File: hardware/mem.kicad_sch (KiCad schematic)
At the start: 3 parts, among them U6 74HC74, U7 28C256, U8 AS6C1008-xxP

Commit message: Added gpio
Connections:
- net GND: now also U6.7 (GND)
- net R/W renamed R/~{W}
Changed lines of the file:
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@@
+		)
+	)
+	(wire
+		(pts
+			(xy 133.35 146.05) (xy 137.16 146.05)
+		)
+		(stroke
+			(width 0)
+			(type default)
 		)
 	)
@@
 		)
 	)
-	(global_label "R{slash}W"
-		(shape input)
-		(at 199.39 93.98 180)
-		(fields_autoplaced yes)
-		(effects
-			(font
-				(size 1.27 1.27)
-			)
-			(justify right)
-		)
-		(property "Intersheetrefs" "${INTERSHEET_REFS}"
-			(at 192.3529 93.98 0)
-			(effects
-				(font
-					(size 1.27 1.27)
-				)
-				(justify right)
-				(hide yes)
-			)
-		)
-	)
 	(global_label "RAM_CS"
 		(shape input)
@@
 	)
 	(global_label "D[0..7]"
-		(shape input)
+		(shape bidirectional)
 		(at 68.58 106.68 180)
 		(fields_autoplaced yes)
@@
 		)
 		(property "Intersheetrefs" "${INTERSHEET_REFS}"
-			(at 59.0028 106.68 0)
+			(at 57.8915 106.68 0)
 			(effects
 				(font
@@
 			(effects
 				(font
+					(size 1.27 1.27)
+				)
+				(justify right)
+				(hide yes)
+			)
+		)
+	)
+	(global_label "R{slash}~{W}"
+		(shape input)
+		(at 199.39 93.98 180)
+		(fields_autoplaced yes)
+		(effects
+			(font
+				(size 1.27 1.27)
+			)
+			(justify right)
+		)
+		(property "Intersheetrefs" "${INTERSHEET_REFS}"
+			(at 192.3529 93.98 0)
+			(effects
+				(font

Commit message: Improved labels
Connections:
- net BANK0 renamed BANK_{0}
- net BANK1 renamed BANK_{1}
- net Bank_CS renamed BANK_{CS}
- net RAM_CS renamed RAM_{~{CS}}
- net ROM_CS renamed ROM_{~{CS}}
- no-connect marks 0 -> 2
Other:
- moved on the sheet: U6A, U6B, U6C

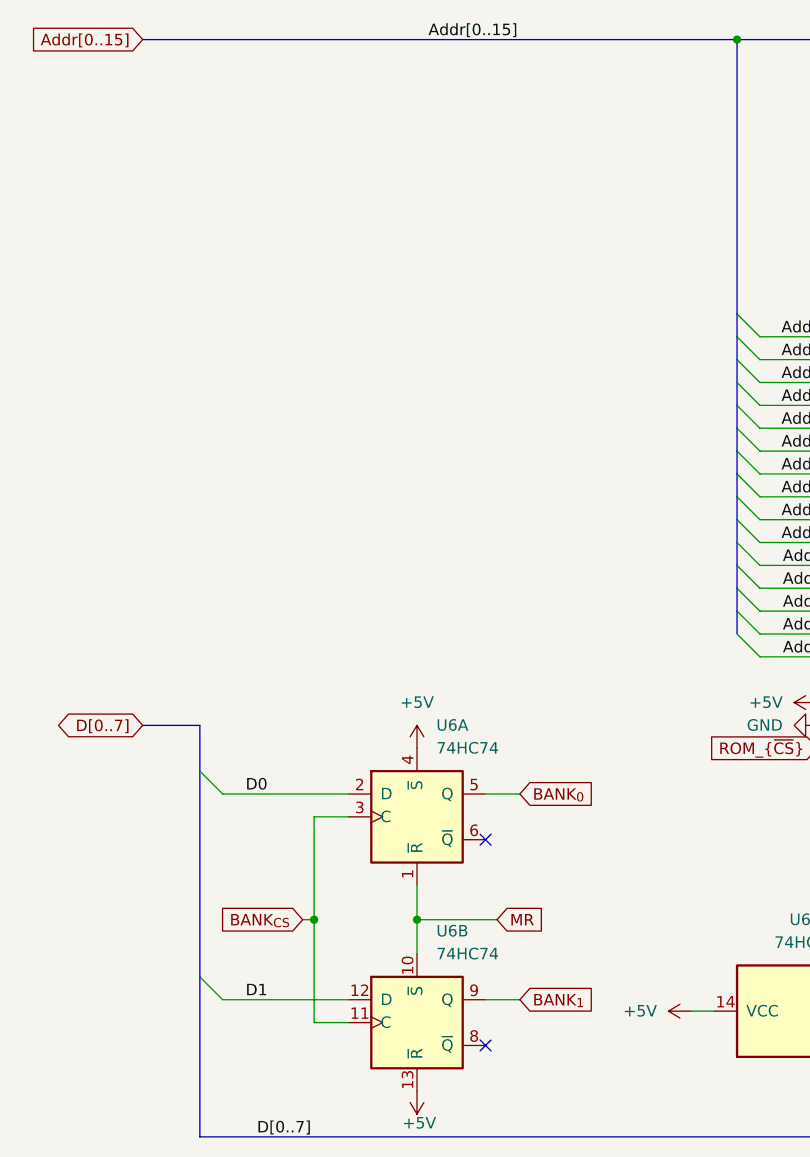
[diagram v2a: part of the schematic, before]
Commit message: Improved Schematics and added fooprints
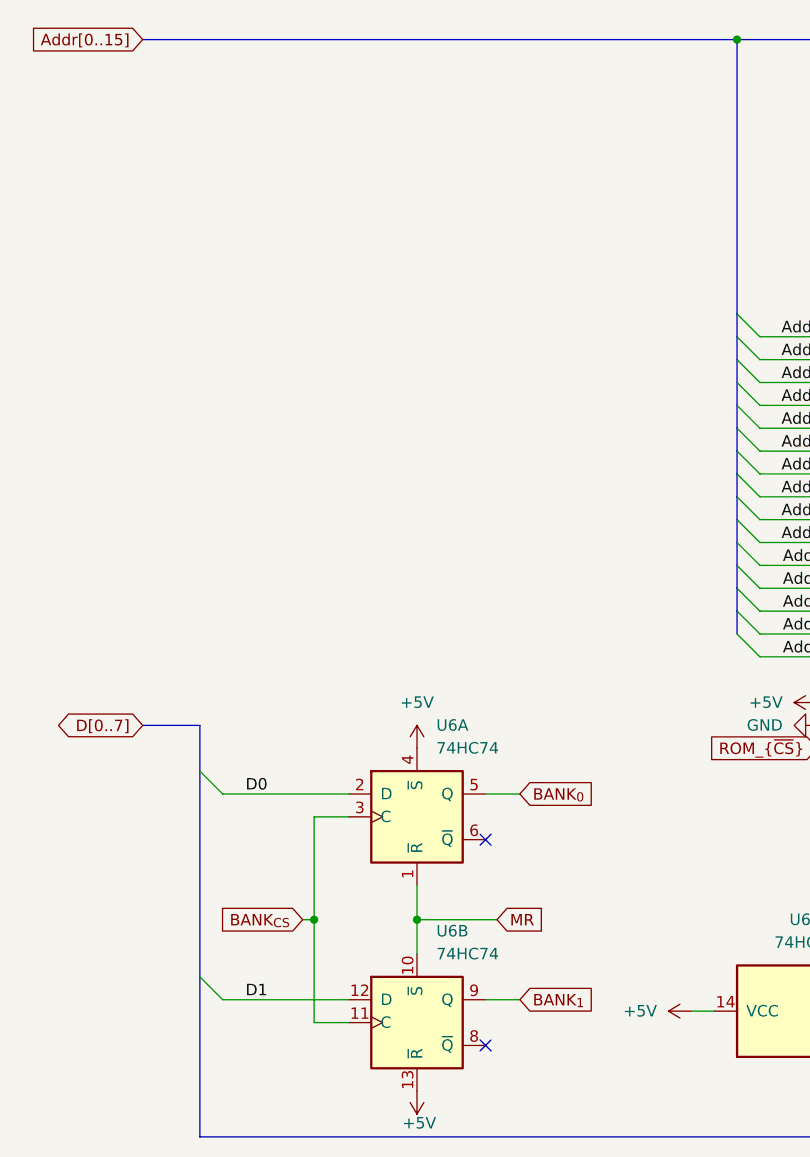
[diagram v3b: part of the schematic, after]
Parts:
- U6: footprint (none) -> Package_DIP:DIP-14_W7.62mm
- U7: footprint (none) -> AT28C256-15PU:DIP1544W45P254L3740H635Q28B
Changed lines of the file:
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@@
-		)
-	)
-	(label "D[0..7]"
-		(at 81.28 152.4 0)
-		(effects
-			(font
-				(size 1.27 1.27)
-			)
-			(justify left bottom)
 		)
 	)
@@
 			)
 			(justify right bottom)
-		)
-	)
-	(label "Addr[0..15]"
-		(at 100.33 30.48 0)
-		(effects
-			(font
-				(size 1.27 1.27)
-			)
-			(justify left bottom)
 		)
 	)
@@
 			)
 		)
-		(property "Footprint" ""
+		(property "Footprint" "Package_DIP:DIP-14_W7.62mm"
 			(at 142.24 138.43 0)
 			(effects
@@
 			)
 		)
-		(property "Footprint" ""
+		(property "Footprint" "Package_DIP:DIP-14_W7.62mm"
 			(at 99.06 116.84 0)
 			(effects
@@
 			)
 		)
-		(property "Footprint" ""
+		(property "Footprint" "AT28C256-15PU:DIP1544W45P254L3740H635Q28B"
 			(at 156.21 86.36 0)
 			(effects
@@
 			)
 		)
-		(property "Footprint" ""
+		(property "Footprint" "Package_DIP:DIP-14_W7.62mm"
 			(at 99.06 139.7 0)
 			(effects

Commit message: Added Board Register
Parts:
- removed U6: 74HC74, Package_DIP:DIP-14_W7.62mm, symbol 74xx:74HC74
- added U12: 74HC373, symbol 74xx:74HC373
- added U13: 74HCT541, symbol 74xx:74HCT541
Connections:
- net D0: now also U12.3 (D0), U13.18 (Y0)
- net D1: now also U12.4 (D1), U13.17 (Y1)
- net D2: now also U12.7 (D2), U13.16 (Y2)
- net D3: now also U12.8 (D3), U13.15 (Y3)
- net D4: now also U12.13 (D4), U13.14 (Y4)
- net D5: now also U12.14 (D5), U13.13 (Y5)
- net D6: now also U12.17 (D6), U13.12 (Y6)
- net D7: now also U12.18 (D7), U13.11 (Y7)
- net GND: now also U12.10 (GND), U13.10 (GND)
- net BANK_{0} renamed Bank_{0}
- net Bank_{0}: now also U12.2 (O0), U13.2 (A0)
- net BANK_{1} renamed Bank_{1}
- net Bank_{1}: now also U12.5 (O1), U13.3 (A1)
- new net: U12.9 (O3), U13.5 (A3)
- new net: U12.12 (O4), U13.6 (A4)
- new net: U12.15 (O5), U13.7 (A5)
- new net: U12.16 (O6), U13.8 (A6)
- new net: U12.19 (O7), U13.9 (A7)
- new net +3.3V: U12.1 (OE), U12.20 (VCC), U13.20 (VCC)
- new net BoardReg_{~{CS}}: U13.1 (G1)
- new net VBank_{2}: U12.6 (O2), U13.4 (A2)
- new net ~{R}/W: U12.11 (LE), U13.19 (G2)
- no-connect marks 2 -> 0

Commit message: Fixed some erros, changed to 3V
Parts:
- added D1, D2, D3, D4, D5, D6, D7, D8: LED, LED_SMD:LED_0805_2012Metric, symbol Device:LED
- added R16, R18, R19, R20, R21, R22, R23, R24: 470R, Resistor_SMD:R_0603_1608Metric, symbol Device:R_Small_US
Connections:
- net +3.3V: now also U7.28 (VCC), U8.32 (VCC)
- net +5V: no longer U7.28 (VCC), U8.32 (VCC)
- net Bank_{0}: now also D1.2 (A)
- net Bank_{1}: now also D2.2 (A)
- net GND: now also R16.2, R18.2, R19.2, R20.2, R21.2, R22.2, R23.2, R24.2
- net BoardReg3: now reaches U12.9 (O3), U13.5 (A3)
- net BoardReg3: now also D4.2 (A)
- net BoardReg4: now reaches U12.12 (O4), U13.6 (A4)
- net BoardReg4: now also D5.2 (A)
- net BoardReg5: now reaches U12.15 (O5), U13.7 (A5)
- net BoardReg5: now also D6.2 (A)
- net BoardReg6: now reaches U12.16 (O6), U13.8 (A6)
- net BoardReg6: now also D7.2 (A)
- net BoardReg7: now reaches U12.19 (O7), U13.9 (A7)
- net BoardReg7: now also D8.2 (A)
- net VBank_{2} renamed BoardReg2
- net BoardReg2: now also D3.2 (A)
- new net: D4.1 (K), R20.1
- new net: D5.1 (K), R18.1
- new net: D8.1 (K), R24.1
- new net: D7.1 (K), R19.1
- new net: D2.1 (K), R22.1
- new net: D3.1 (K), R21.1
- new net: D6.1 (K), R16.1
- new net: D1.1 (K), R23.1

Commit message: Fixed all erros and warning
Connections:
- net +5V is gone; now on net +3.3V: U7.27 (~{WE}), U8.30 (CS2/CE2)
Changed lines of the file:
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@@
 		)
 	)
-	(wire
-		(pts
-			(xy 143.51 104.14) (xy 146.05 104.14)
-		)
-		(stroke
-			(width 0)
-			(type default)
-		)
-	)
 	(bus
 		(pts
@@
 	(wire
 		(pts
+			(xy 196.85 88.9) (xy 203.2 88.9)
+		)
+		(stroke
+			(width 0)
+			(type default)
+		)
+	)
+	(wire
+		(pts
 			(xy 102.87 52.07) (xy 100.33 52.07)
 		)
@@
 	(wire
 		(pts
-			(xy 198.12 88.9) (xy 203.2 88.9)
-		)
-		(stroke
-			(width 0)
-			(type default)
-		)
-	)
-	(wire
-		(pts
 			(xy 179.07 71.12) (xy 203.2 71.12)
 		)
@@
 		)
 	)
+	(wire
+		(pts
+			(xy 142.24 104.14) (xy 146.05 104.14)
+		)
+		(stroke
+			(width 0)
+			(type default)
+		)
+	)
 	(bus
 		(pts
@@
 	)
 	(symbol
-		(lib_id "power:+5V")
-		(at 198.12 88.9 90)
-		(unit 1)
-		(exclude_from_sim no)
-		(in_bom yes)
-		(on_board yes)
-		(dnp no)
-		(fields_autoplaced yes)
-		(property "Reference" "#PWR028"
-			(at 201.93 88.9 0)
-			(effects
-				(font
-					(size 1.27 1.27)
-				)
-				(hide yes)
-			)
-		)
-		(property "Value" "+5V"
-			(at 194.31 88.8999 90)
-			(effects
-				(font
-					(size 1.27 1.27)
-				)
-				(justify left)
-			)
-		)
-		(property "Footprint" ""
-			(at 198.12 88.9 0)
-			(effects
-				(font
-					(size 1.27 1.27)
-				)
-				(hide yes)
-			)
-		)
-		(property "Datasheet" ""
-			(at 198.12 88.9 0)
-			(effects
-				(font
-					(size 1.27 1.27)
-				)
-				(hide yes)
-			)
-		)
-		(property "Description" "Power symbol creates a global label with name \"+5V\""
-			(at 198.12 88.9 0)
-			(effects
-				(font
-					(size 1.27 1.27)
-				)
-				(hide yes)
-			)
-		)
-		(pin "1"
-		)
-		(instances
-			(project "Lambda One"
-				(path "/73ea9964-373f-4fdc-b03e-f532cf836c0d/393dc2fd-ccc9-40ef-ba1b-4142573d9a3b"
-					(reference "#PWR028")
-					(unit 1)
-				)
-			)
-		)
-	)
-	(symbol
 		(lib_id "Device:R_Small_US")
 		(at 97.79 57.15 90)
@@
 	)
 	(symbol
+		(lib_id "power:+3.3V")
+		(at 142.24 104.14 90)
+		(unit 1)
+		(exclude_from_sim no)
+		(in_bom yes)
+		(on_board yes)
+		(dnp no)
+		(property "Reference" "#PWR024"
+			(at 146.05 104.14 0)
+			(effects
+				(font
+					(size 1.27 1.27)
+				)
+				(hide yes)
+			)
+		)
+		(property "Value" "+3.3V"
+			(at 137.16 104.14 90)
+			(effects
+				(font
+					(size 1.27 1.27)
+				)
+			)
+		)
+		(property "Footprint" ""
+			(at 142.24 104.14 0)
+			(effects
+				(font
+					(size 1.27 1.27)
+				)
+				(hide yes)
+			)
+		)
+		(property "Datasheet" ""
+			(at 142.24 104.14 0)
+			(effects
+				(font
+					(size 1.27 1.27)
+				)
+				(hide yes)
+			)
+		)
+		(property "Description" "Power symbol creates a global label with name \"+3.3V\""
+			(at 142.24 104.14 0)
+			(effects
+				(font
+					(size 1.27 1.27)
+				)
+				(hide yes)
+			)
+		)
+		(pin "1"
+		)
+		(instances
+			(project "Lambda One"
+				(path "/73ea9964-373f-4fdc-b03e-f532cf836c0d/393dc2fd-ccc9-40ef-ba1b-4142573d9a3b"
+					(reference "#PWR024")
+					(unit 1)
+				)
+			)
+		)
+	)
+	(symbol
 		(lib_id "Device:R_Small_US")
 		(at 97.79 52.07 90)
@@
 	)
 	(symbol
-		(lib_id "power:+5V")
-		(at 143.51 104.14 90)
+		(lib_id "Device:LED")
+		(at 87.63 62.23 180)
 		(unit 1)
 		(exclude_from_sim no)
@@
 		(on_board yes)
 		(dnp no)
-		(fields_autoplaced yes)
-		(property "Reference" "#PWR024"
-			(at 147.32 104.14 0)
+		(property "Reference" "D3"
+			(at 84.836 60.198 0)
 			(effects
 				(font
 					(size 1.27 1.27)
 				)
-				(hide yes)
 			)
 		)
-		(property "Value" "+5V"
-			(at 139.7 104.1399 90)
+		(property "Value" "LED"
+			(at 87.884 59.436 0)
 			(effects
 				(font
 					(size 1.27 1.27)
 				)
-				(justify left)
 			)
 		)
-		(property "Footprint" ""
-			(at 143.51 104.14 0)
+		(property "Footprint" "LED_SMD:LED_0805_2012Metric"
+			(at 87.63 62.23 0)
 			(effects
 				(font
@@
 			)
 		)
-		(property "Datasheet" ""
-			(at 143.51 104.14 0)
+		(property "Datasheet" "~"
+			(at 87.63 62.23 0)
+			(effects
+				(font
+					(size 1.27 1.27)
+				)
+				(hide yes)
+			)
+		)
+		(property "Description" "Light emitting diode"
+			(at 87.63 62.23 0)
 			(effects
 				(font
@@
 			)
 		)
-		(property "Description" "Power symbol creates a global label with name \"+5V\""
-			(at 143.51 104.14 0)
+		(property "Sim.Pins" "1=K 2=A"
+			(at 87.63 62.23 0)
 			(effects
 				(font
@@
 		(pin "1"
 		)
+		(pin "2"
+		)
 		(instances
 			(project "Lambda One"
 				(path "/73ea9964-373f-4fdc-b03e-f532cf836c0d/393dc2fd-ccc9-40ef-ba1b-4142573d9a3b"
-					(reference "#PWR024")
+					(reference "D3")
 					(unit 1)
 				)
@@
 	(symbol
 		(lib_id "Device:LED")
-		(at 87.63 62.23 180)
+		(at 87.63 77.47 180)
 		(unit 1)
 		(exclude_from_sim no)
@@
 		(on_board yes)
 		(dnp no)
-		(property "Reference" "D3"
-			(at 84.836 60.198 0)
+		(property "Reference" "D6"
+			(at 84.836 75.438 0)
 			(effects
 				(font
@@
 		)
 		(property "Value" "LED"
-			(at 87.884 59.436 0)
+			(at 87.884 74.676 0)
 			(effects
 				(font
@@
 		)
 		(property "Footprint" "LED_SMD:LED_0805_2012Metric"
-			(at 87.63 62.23 0)
+			(at 87.63 77.47 0)
 			(effects
 				(font
@@
 		)
 		(property "Datasheet" "~"
-			(at 87.63 62.23 0)
+			(at 87.63 77.47 0)
 			(effects
 				(font
@@
 		)
 		(property "Description" "Light emitting diode"
-			(at 87.63 62.23 0)
+			(at 87.63 77.47 0)
 			(effects
 				(font
@@
 		)
 		(property "Sim.Pins" "1=K 2=A"
-			(at 87.63 62.23 0)
+			(at 87.63 77.47 0)
 			(effects
 				(font
@@
 			(project "Lambda One"
 				(path "/73ea9964-373f-4fdc-b03e-f532cf836c0d/393dc2fd-ccc9-40ef-ba1b-4142573d9a3b"
-					(reference "D3")
+					(reference "D6")
 					(unit 1)
 				)
@@
 	)
 	(symbol
-		(lib_id "Device:LED")
-		(at 87.63 77.47 180)
+		(lib_id "power:+3.3V")
+		(at 215.9 55.88 0)
 		(unit 1)
 		(exclude_from_sim no)
@@
 		(on_board yes)
 		(dnp no)
-		(property "Reference" "D6"
-			(at 84.836 75.438 0)
-			(effects
-				(font
-					(size 1.27 1.27)
-				)
-			)
-		)
-		(property "Value" "LED"
-			(at 87.884 74.676 0)
+		(property "Reference" "#PWR030"
+			(at 215.9 59.69 0)
 			(effects
 				(font
 					(size 1.27 1.27)
 				)
+				(hide yes)
 			)
 		)
-		(property "Footprint" "LED_SMD:LED_0805_2012Metric"
-			(at 87.63 77.47 0)
+		(property "Value" "+3.3V"
+			(at 215.9 50.8 0)
 			(effects
 				(font
 					(size 1.27 1.27)
 				)
-				(hide yes)
 			)
 		)
-		(property "Datasheet" "~"
-			(at 87.63 77.47 0)
+		(property "Footprint" ""
+			(at 215.9 55.88 0)
 			(effects
 				(font
@@
 			)
 		)
-		(property "Description" "Light emitting diode"
-			(at 87.63 77.47 0)
+		(property "Datasheet" ""
+			(at 215.9 55.88 0)
 			(effects
 				(font
@@
 			)
 		)
-		(property "Sim.Pins" "1=K 2=A"
-			(at 87.63 77.47 0)
+		(property "Description" "Power symbol creates a global label with name \"+3.3V\""
+			(at 215.9 55.88 0)
 			(effects
 				(font
@@
 		(pin "1"
 		)
-		(pin "2"
-		)
 		(instances
 			(project "Lambda One"
 				(path "/73ea9964-373f-4fdc-b03e-f532cf836c0d/393dc2fd-ccc9-40ef-ba1b-4142573d9a3b"
-					(reference "D6")
+					(reference "#PWR030")
 					(unit 1)
 				)
@@
 	(symbol
 		(lib_id "power:+3.3V")
-		(at 215.9 55.88 0)
+		(at 196.85 88.9 90)
 		(unit 1)
 		(exclude_from_sim no)
@@
 		(on_board yes)
 		(dnp no)
-		(property "Reference" "#PWR030"
-			(at 215.9 59.69 0)
+		(property "Reference" "#PWR028"
+			(at 200.66 88.9 0)
 			(effects
 				(font
@@
 		)
 		(property "Value" "+3.3V"
-			(at 215.9 50.8 0)
+			(at 191.77 88.9 90)
 			(effects
 				(font
@@
 		)
 		(property "Footprint" ""
-			(at 215.9 55.88 0)
+			(at 196.85 88.9 0)
 			(effects
 				(font
@@
 		)
 		(property "Datasheet" ""
-			(at 215.9 55.88 0)
+			(at 196.85 88.9 0)
 			(effects
 				(font
@@
 		)
 		(property "Description" "Power symbol creates a global label with name \"+3.3V\""
-			(at 215.9 55.88 0)
+			(at 196.85 88.9 0)
 			(effects
 				(font
@@
 			(project "Lambda One"
 				(path "/73ea9964-373f-4fdc-b03e-f532cf836c0d/393dc2fd-ccc9-40ef-ba1b-4142573d9a3b"
-					(reference "#PWR030")
+					(reference "#PWR028")
 					(unit 1)
 				)
